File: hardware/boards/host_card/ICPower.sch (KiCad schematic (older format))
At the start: 48 parts, among them J6 SODIMM_260, U1 ECP5UM5G-381caBGA, U3 CYUSB3014, U4 IS43TR16256B-125KBL, U5 128MiB, U6 128MiB, U7 SI5330B

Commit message: Updated the generic SODIMM part footprint to use the new Debug Module footprint
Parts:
- J6: footprint lethalbit-connectors:TE_SODIMM_260 -> lethalbit-connectors:lethallink_Debug_Module_Mount
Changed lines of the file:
@@
 F 0 "J6" H 14400 3525 50  0000 C CNN
 F 1 "SODIMM_260" H 14400 3434 50  0000 C CNN
-F 2 "lethalbit-connectors:TE_SODIMM_260" H 14400 3300 50  0001 C CNN
+F 2 "lethalbit-connectors:lethallink_Debug_Module_Mount" H 14400 3300 50  0001 C CNN
 F 3 "https://www.te.com/commerce/DocumentDelivery/DDEController?Action=srchrtrv&DocNm=2309413&DocType=Customer+Drawing&DocLang=English" H 14400 3300 50  0001 C CNN
 F 4 "TE Connectivity AMP Connectors" H 14400 2950 50  0001 C CNN "MFR"
@@
 F 0 "J6" H 14400 7275 50  0000 C CNN
 F 1 "SODIMM_260" H 14400 7184 50  0000 C CNN
-F 2 "lethalbit-connectors:TE_SODIMM_260" H 14400 7050 50  0001 C CNN
+F 2 "lethalbit-connectors:lethallink_Debug_Module_Mount" H 14400 7050 50  0001 C CNN
 F 3 "https://www.te.com/commerce/DocumentDelivery/DDEController?Action=srchrtrv&DocNm=2309413&DocType=Customer+Drawing&DocLang=English" H 14400 7050 50  0001 C CNN
 F 4 "TE Connectivity AMP Connectors" H 14400 6700 50  0001 C CNN "MFR"

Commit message: Some updates with the debug module interface
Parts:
- J6: footprint lethalbit-connectors:lethallink_Debug_Module_Mount -> lethallink:lethallink_debug_module_mount
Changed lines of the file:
@@
 F 0 "J6" H 14400 3525 50  0000 C CNN
 F 1 "SODIMM_260" H 14400 3434 50  0000 C CNN
-F 2 "lethalbit-connectors:lethallink_Debug_Module_Mount" H 14400 3300 50  0001 C CNN
+F 2 "lethallink:lethallink_debug_module_mount" H 14400 3300 50  0001 C CNN
 F 3 "https://www.te.com/commerce/DocumentDelivery/DDEController?Action=srchrtrv&DocNm=2309413&DocType=Customer+Drawing&DocLang=English" H 14400 3300 50  0001 C CNN
 F 4 "TE Connectivity AMP Connectors" H 14400 2950 50  0001 C CNN "MFR"
@@
 F 0 "J6" H 14400 7275 50  0000 C CNN
 F 1 "SODIMM_260" H 14400 7184 50  0000 C CNN
-F 2 "lethalbit-connectors:lethallink_Debug_Module_Mount" H 14400 7050 50  0001 C CNN
+F 2 "lethallink:lethallink_debug_module_mount" H 14400 7050 50  0001 C CNN
 F 3 "https://www.te.com/commerce/DocumentDelivery/DDEController?Action=srchrtrv&DocNm=2309413&DocType=Customer+Drawing&DocLang=English" H 14400 7050 50  0001 C CNN
 F 4 "TE Connectivity AMP Connectors" H 14400 6700 50  0001 C CNN "MFR"

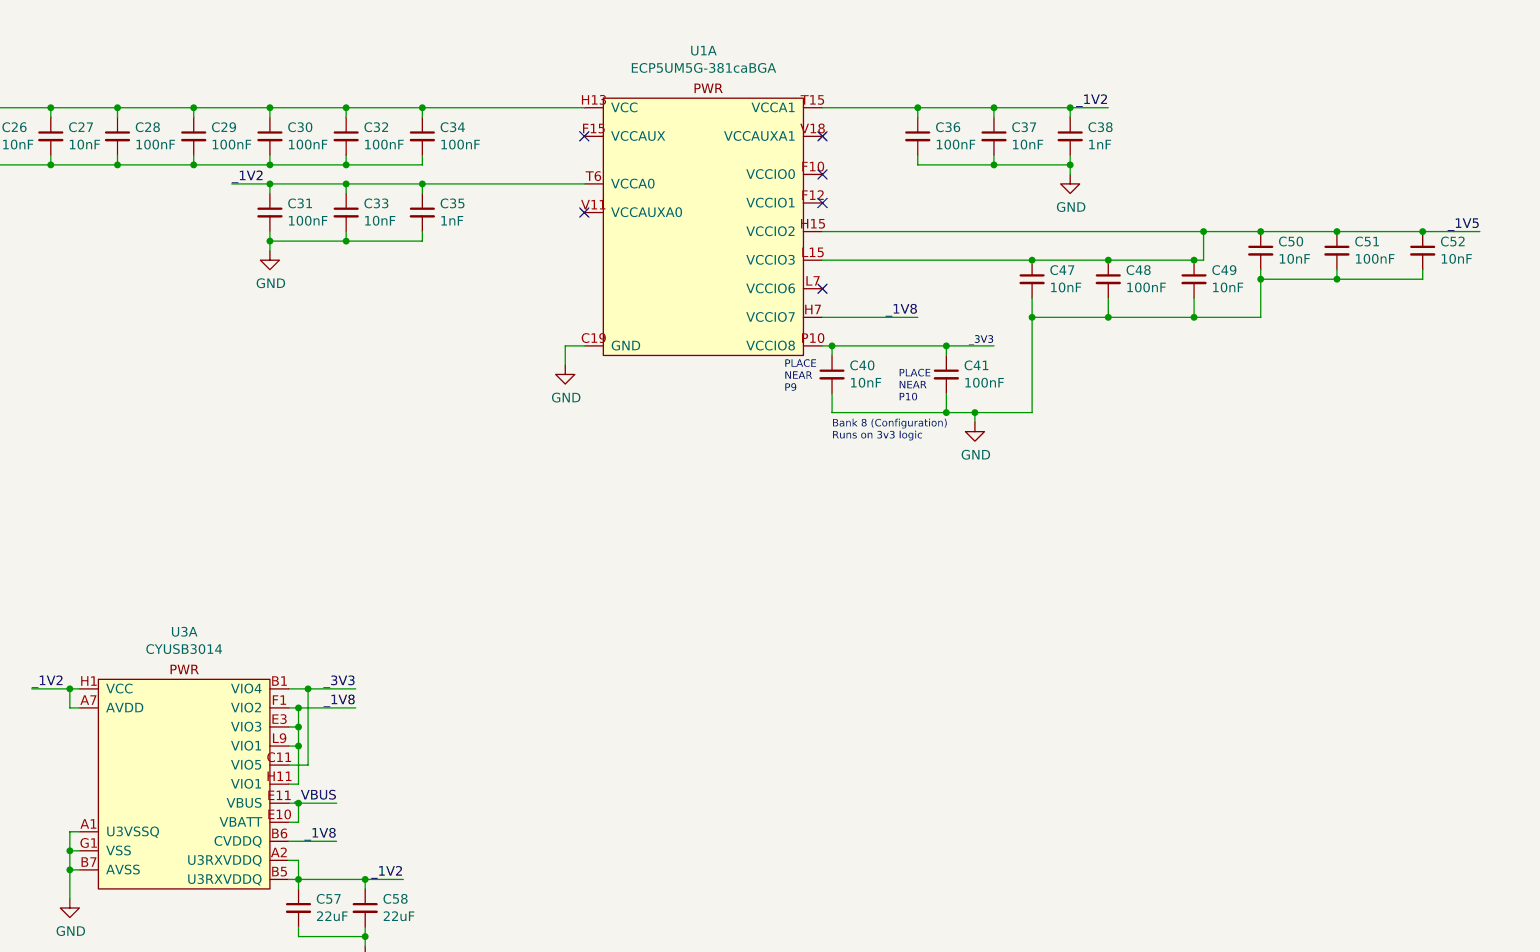
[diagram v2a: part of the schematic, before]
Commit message: Fixed up the consistancy of value naming, 100nF -> 0.1uF. Added the caps for the USB SSRX lines, moved the Ferrite for VBUS to fix a net naming issue
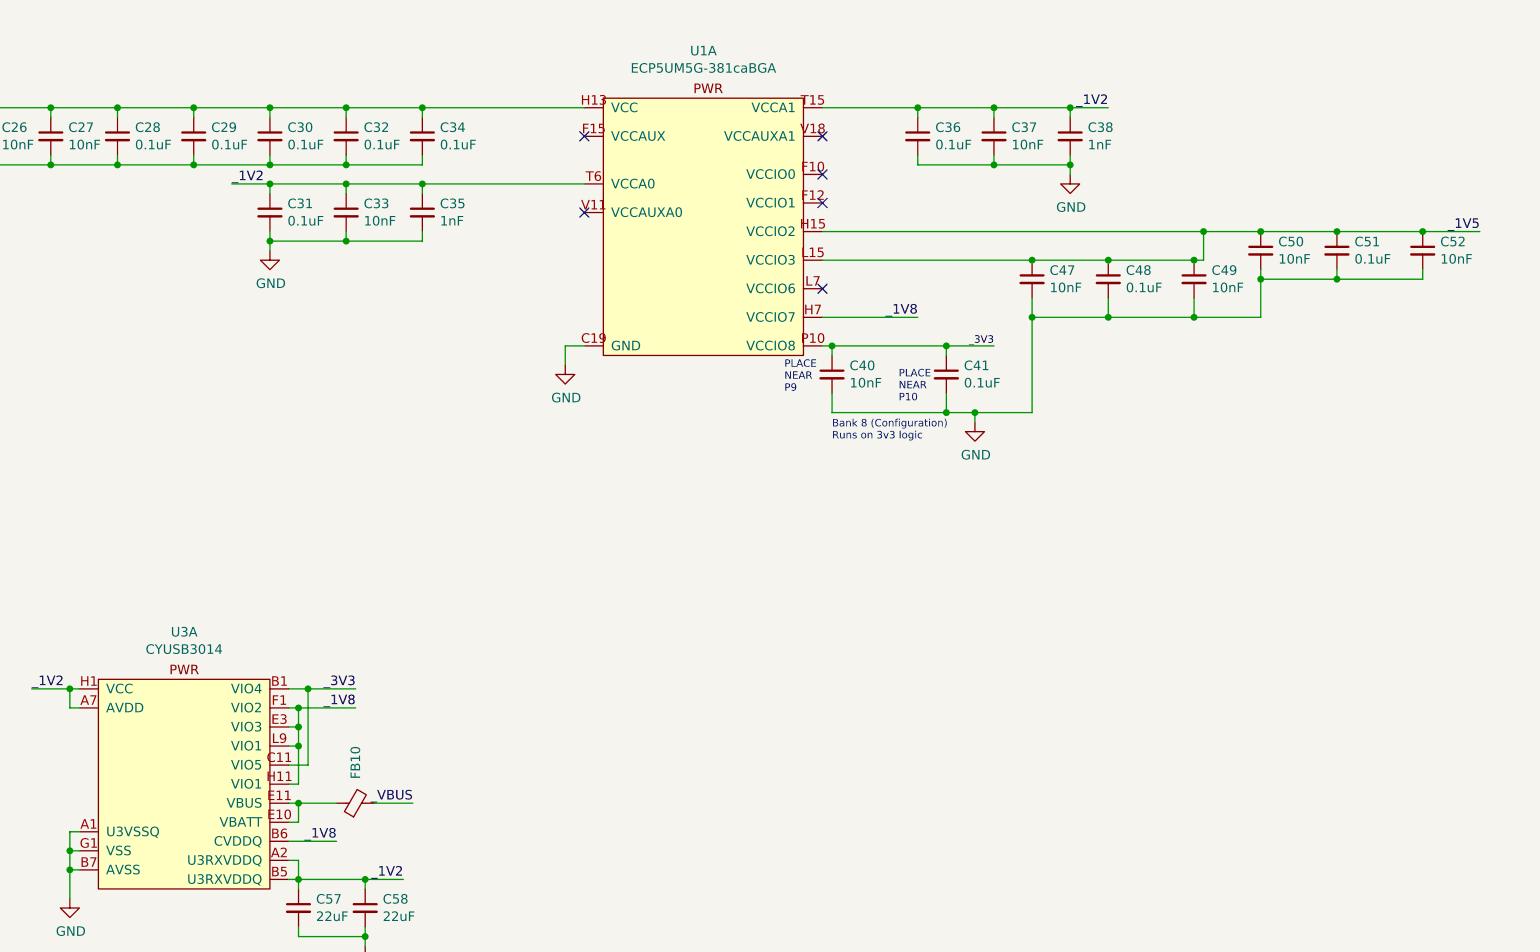
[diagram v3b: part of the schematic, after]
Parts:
- added FB10: 220 @ 100Mhz, Resistor_SMD:R_0603_1608Metric, symbol Device:Ferrite_Bead_Small
- C28, C29, C30, C31, C32, C34, C36, C41, C48, C51: value 100nF -> 0.1uF
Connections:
- net VBUS: now also FB10.2; no longer U3.E10 (VBATT), U3.E11 (VBUS)
- new net: FB10.1, U3.E10 (VBATT), U3.E11 (VBUS)
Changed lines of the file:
@@
 P 6200 2200
 F 0 "C31" H 6292 2246 50  0000 L CNN
-F 1 "100nF" H 6292 2155 50  0000 L CNN
+F 1 "0.1uF" H 6292 2155 50  0000 L CNN
 F 2 "Capacitor_SMD:C_0402_1005Metric" H 6200 2200 50  0001 C CNN
 F 3 "~" H 6200 2200 50  0001 C CNN
@@
 P 9600 1800
 F 0 "C36" H 9692 1846 50  0000 L CNN
-F 1 "100nF" H 9692 1755 50  0000 L CNN
+F 1 "0.1uF" H 9692 1755 50  0000 L CNN
 F 2 "Capacitor_SMD:C_0402_1005Metric" H 9600 1800 50  0001 C CNN
 F 3 "~" H 9600 1800 50  0001 C CNN
@@
 P 7000 1800
 F 0 "C34" H 7092 1846 50  0000 L CNN
-F 1 "100nF" H 7092 1755 50  0000 L CNN
+F 1 "0.1uF" H 7092 1755 50  0000 L CNN
 F 2 "Capacitor_SMD:C_0402_1005Metric" H 7000 1800 50  0001 C CNN
 F 3 "~" H 7000 1800 50  0001 C CNN
@@
 P 6600 1800
 F 0 "C32" H 6692 1846 50  0000 L CNN
-F 1 "100nF" H 6692 1755 50  0000 L CNN
+F 1 "0.1uF" H 6692 1755 50  0000 L CNN
 F 2 "Capacitor_SMD:C_0402_1005Metric" H 6600 1800 50  0001 C CNN
 F 3 "~" H 6600 1800 50  0001 C CNN
@@
 P 6200 1800
 F 0 "C30" H 6292 1846 50  0000 L CNN
-F 1 "100nF" H 6292 1755 50  0000 L CNN
+F 1 "0.1uF" H 6292 1755 50  0000 L CNN
 F 2 "Capacitor_SMD:C_0402_1005Metric" H 6200 1800 50  0001 C CNN
 F 3 "~" H 6200 1800 50  0001 C CNN
@@
 P 5800 1800
 F 0 "C29" H 5892 1846 50  0000 L CNN
-F 1 "100nF" H 5892 1755 50  0000 L CNN
+F 1 "0.1uF" H 5892 1755 50  0000 L CNN
 F 2 "Capacitor_SMD:C_0402_1005Metric" H 5800 1800 50  0001 C CNN
 F 3 "~" H 5800 1800 50  0001 C CNN
@@
 P 5400 1800
 F 0 "C28" H 5492 1846 50  0000 L CNN
-F 1 "100nF" H 5492 1755 50  0000 L CNN
+F 1 "0.1uF" H 5492 1755 50  0000 L CNN
 F 2 "Capacitor_SMD:C_0402_1005Metric" H 5400 1800 50  0001 C CNN
 F 3 "~" H 5400 1800 50  0001 C CNN
@@
 P 9750 3050
 F 0 "C41" H 9842 3096 50  0000 L CNN
-F 1 "100nF" H 9842 3005 50  0000 L CNN
+F 1 "0.1uF" H 9842 3005 50  0000 L CNN
 F 2 "Capacitor_SMD:C_0402_1005Metric" H 9750 3050 50  0001 C CNN
 F 3 "~" H 9750 3050 50  0001 C CNN
@@
 Wire Wire Line
 	6300 5300 6350 5300
-Text Label 6550 5300 2    50   ~ 0
-_VBUS
 $Comp
 L power:GND #PWR0124
@@
 P 10600 2550
 F 0 "C48" H 10692 2596 50  0000 L CNN
-F 1 "100nF" H 10692 2505 50  0000 L CNN
+F 1 "0.1uF" H 10692 2505 50  0000 L CNN
 F 2 "Capacitor_SMD:C_0402_1005Metric" H 10600 2550 50  0001 C CNN
 F 3 "~" H 10600 2550 50  0001 C CNN
@@
 P 11800 2400
 F 0 "C51" H 11892 2446 50  0000 L CNN
-F 1 "100nF" H 11892 2355 50  0000 L CNN
+F 1 "0.1uF" H 11892 2355 50  0000 L CNN
 F 2 "Capacitor_SMD:C_0402_1005Metric" H 11800 2400 50  0001 C CNN
 F 3 "~" H 11800 2400 50  0001 C CNN
@@
 Wire Wire Line
 	6350 5400 6300 5400
-Connection ~ 6350 5300
-Wire Wire Line
-	6350 5300 6550 5300
 Wire Wire Line
 	6300 5100 6400 5100
@@
 	1    0    0    -1
 $EndComp
+$Comp
+L Device:Ferrite_Bead_Small FB?
+U 1 1 5F3AE682
+P 6650 5300
+AR Path="/5F3AE682" Ref="FB?"  Part="1"
+AR Path="/5EF66188/5F3AE682" Ref="FB10"  Part="1"
+F 0 "FB10" H 6950 5300 50  0000 R CNN
+F 1 "220 @ 100Mhz" H 6800 5500 50  0001 R CNN
+F 2 "Resistor_SMD:R_0603_1608Metric" V 6580 5300 50  0001 C CNN
+F 3 "~" H 6650 5300 50  0001 C CNN
+F 4 "Murata Electronics" H 6650 5300 50  0001 C CNN "MFR"
+F 5 "BLM18AG221SN1D" H 6650 5300 50  0001 C CNN "MPN"
+	1    6650 5300
+	0    -1   -1   0
+$EndComp
+Text Label 6950 5300 2    50   ~ 0
+_VBUS
+Wire Wire Line
+	6750 5300 6950 5300
+Wire Wire Line
+	6350 5300 6550 5300
+Connection ~ 6350 5300
 $EndSCHEMATC

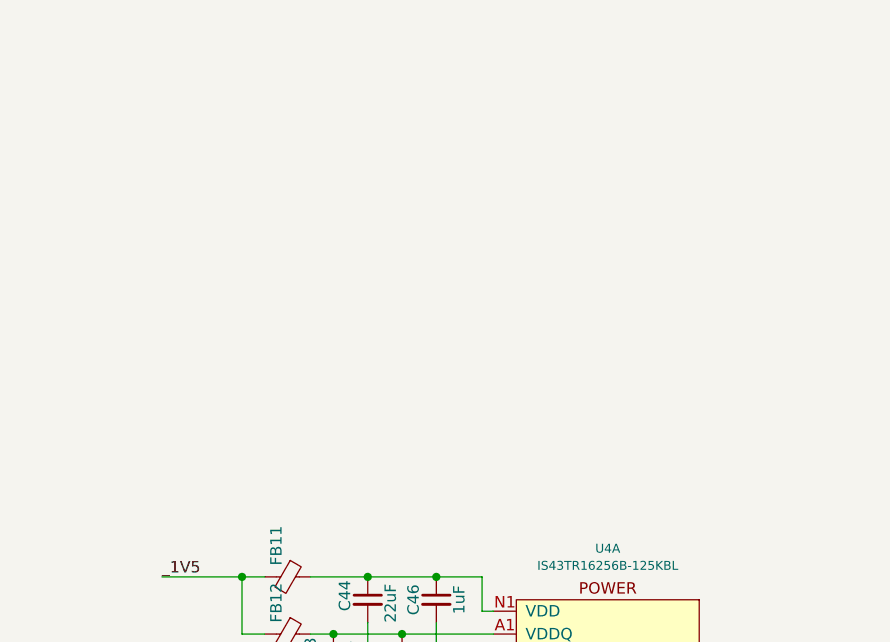
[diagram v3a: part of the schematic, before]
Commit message: Added another DDR3 module to expand cache to 8GiB
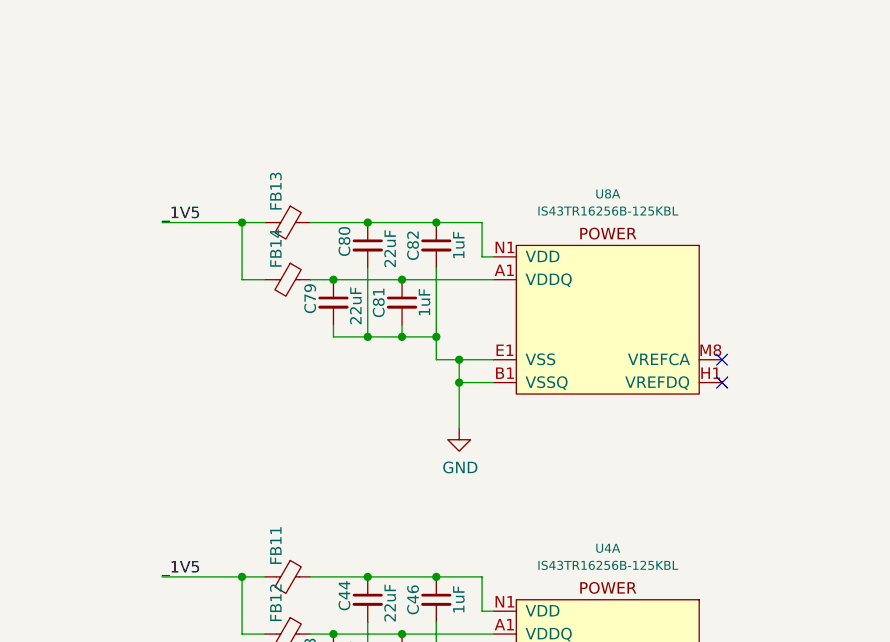
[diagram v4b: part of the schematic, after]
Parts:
- added C79, C80: 22uF, Capacitor_SMD:C_1206_3216Metric, symbol Device:C_Small
- added C81, C82: 1uF, Capacitor_SMD:C_0603_1608Metric, symbol Device:C_Small
- added FB13, FB14: 220 @ 100Mhz, Resistor_SMD:R_0603_1608Metric, symbol Device:Ferrite_Bead_Small
- added U8: IS43TR16256B-125KBL, Package_BGA:BGA-96_9.0x13.0mm_Layout2x3x16_P0.8mm, symbol lethalbit-memory:IS43TR16256B-125KBL
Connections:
- net 1V5: now also FB13.2, FB14.2
- net GND: now also C79.2, C80.2, C81.2, C82.2, U8.A9 (VSS), U8.B1 (VSSQ), U8.B3 (VSS), U8.B9 (VSSQ), U8.D1 (VSSQ), U8.D8 (VSSQ), U8.E1 (VSS), U8.E2 (VSSQ), U8.E8 (VSSQ), U8.F9 (VSSQ), U8.G1 (VSSQ), U8.G8 (VSS), U8.G9 (VSSQ), U8.J2 (VSS), U8.J8 (VSS), U8.M1 (VSS), U8.M9 (VSS), U8.P1 (VSS), U8.P9 (VSS), U8.T1 (VSS), U8.T9 (VSS)
- new net: C79.1, C81.1, FB14.1, U8.A1 (VDDQ), U8.A8 (VDDQ), U8.C1 (VDDQ), U8.C9 (VDDQ), U8.D2 (VDDQ), U8.E9 (VDDQ), U8.F1 (VDDQ), U8.H2 (VDDQ), U8.H9 (VDDQ)
- new net: C80.1, C82.1, FB13.1, U8.B2 (VDD), U8.D9 (VDD), U8.G7 (VDD), U8.K2 (VDD), U8.K8 (VDD), U8.N1 (VDD), U8.N9 (VDD), U8.R1 (VDD), U8.R9 (VDD)
- no-connect marks 8 -> 10
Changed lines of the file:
@@
 	6350 5300 6550 5300
 Connection ~ 6350 5300
+$Comp
+L lethalbit-memory:IS43TR16256B-125KBL U8
+U 1 1 5F484D89
+P 10250 6650
+F 0 "U8" H 10250 7124 39  0000 C CNN
+F 1 "IS43TR16256B-125KBL" H 10250 7049 39  0000 C CNN
+F 2 "Package_BGA:BGA-96_9.0x13.0mm_Layout2x3x16_P0.8mm" H 10250 7050 39  0001 C CNN
+F 3 "http://www.issi.com/WW/pdf/43-46TR16256B-85120BL.pdf" H 10250 7050 39  0001 C CNN
+F 4 "ISSI" H 10250 6650 50  0001 C CNN "MFR"
+F 5 "IS43TR16256B-125KBL" H 10250 6650 50  0001 C CNN "MPN"
+	1    10250 6650
+	1    0    0    -1
+$EndComp
+$Comp
+L power:GND #PWR0145
+U 1 1 5F4B038F
+P 9600 7200
+F 0 "#PWR0145" H 9600 6950 50  0001 C CNN
+F 1 "GND" H 9605 7027 50  0000 C CNN
+F 2 "" H 9600 7200 50  0001 C CNN
+F 3 "" H 9600 7200 50  0001 C CNN
+	1    9600 7200
+	1    0    0    -1
+$EndComp
+Wire Wire Line
+	9750 7000 9600 7000
+Wire Wire Line
+	9600 7000 9600 7200
+Wire Wire Line
+	9750 6900 9600 6900
+Wire Wire Line
+	9600 6900 9600 7000
+Connection ~ 9600 7000
+Wire Wire Line
+	8650 6550 8650 6300
+Wire Wire Line
+	8650 6300 8300 6300
+Text Label 8300 6300 0    50   ~ 0
+_1V5
+Wire Wire Line
+	8750 6550 8650 6550
+Wire Wire Line
+	8650 6300 8750 6300
+Connection ~ 8650 6300
+$Comp
+L Device:Ferrite_Bead_Small FB?
+U 1 1 5F4B03A2
+P 8850 6550
+AR Path="/5F4B03A2" Ref="FB?"  Part="1"
+AR Path="/5EF66188/5F4B03A2" Ref="FB14"  Part="1"
+F 0 "FB14" H 8800 6500 50  0000 R CNN
+F 1 "220 @ 100Mhz" H 9000 6750 50  0001 R CNN
+F 2 "Resistor_SMD:R_0603_1608Metric" V 8780 6550 50  0001 C CNN
+F 3 "~" H 8850 6550 50  0001 C CNN
+F 4 "Murata Electronics" H 8850 6550 50  0001 C CNN "MFR"
+F 5 "BLM18AG221SN1D" H 8850 6550 50  0001 C CNN "MPN"
+	1    8850 6550
+	0    1    1    0
+$EndComp
+$Comp
+L Device:Ferrite_Bead_Small FB?
+U 1 1 5F4B03AA
+P 8850 6300
+AR Path="/5F4B03AA" Ref="FB?"  Part="1"
+AR Path="/5EF66188/5F4B03AA" Ref="FB13"  Part="1"
+F 0 "FB13" H 8800 6250 50  0000 R CNN
+F 1 "220 @ 100Mhz" H 9000 6500 50  0001 R CNN
+F 2 "Resistor_SMD:R_0603_1608Metric" V 8780 6300 50  0001 C CNN
+F 3 "~" H 8850 6300 50  0001 C CNN
+F 4 "Murata Electronics" H 8850 6300 50  0001 C CNN "MFR"
+F 5 "BLM18AG221SN1D" H 8850 6300 50  0001 C CNN "MPN"
+	1    8850 6300
+	0    1    1    0
+$EndComp
+Wire Wire Line
+	8950 6550 9050 6550
+Wire Wire Line
+	9700 6300 9700 6450
+Wire Wire Line
+	9700 6450 9750 6450
+$Comp
+L Device:C_Small C?
+U 1 1 5F4B03B5
+P 9050 6650
+AR Path="/5EDF9F51/5F4B03B5" Ref="C?"  Part="1"
+AR Path="/5EF66188/5F4B03B5" Ref="C79"  Part="1"
+F 0 "C79" V 8950 6600 50  0000 L CNN
+F 1 "22uF" V 9150 6550 50  0000 L CNN
+F 2 "Capacitor_SMD:C_1206_3216Metric" H 9050 6650 50  0001 C CNN
+F 3 "~" H 9050 6650 50  0001 C CNN
+F 4 "KEMET" H 9050 6650 50  0001 C CNN "MFR"
+F 5 "C1206C226K9PACTU" H 9050 6650 50  0001 C CNN "MPN"
+	1    9050 6650
+	1    0    0    -1
+$EndComp
+Connection ~ 9050 6550
+Wire Wire Line
+	9050 6550 9350 6550
+$Comp
+L Device:C_Small C?
+U 1 1 5F4B03BF
+P 9350 6650
+AR Path="/5EDF9F51/5F4B03BF" Ref="C?"  Part="1"
+AR Path="/5EF66188/5F4B03BF" Ref="C81"  Part="1"
+F 0 "C81" V 9250 6650 50  0000 C CNN
+F 1 "1uF" V 9450 6650 50  0000 C CNN
+F 2 "Capacitor_SMD:C_0603_1608Metric" H 9350 6650 50  0001 C CNN
+F 3 "~" H 9350 6650 50  0001 C CNN
+F 4 "KEMET" V 9350 6650 50  0001 C CNN "MFR"
+F 5 "C0603C105K4RACTU" V 9350 6650 50  0001 C CNN "MPN"
+	1    9350 6650
+	1    0    0    -1
+$EndComp
+Connection ~ 9350 6550
+Wire Wire Line
+	9350 6550 9750 6550
+Wire Wire Line
+	8950 6300 9200 6300
+$Comp
+L Device:C_Small C?
+U 1 1 5F4B03CA
+P 9200 6400
+AR Path="/5EDF9F51/5F4B03CA" Ref="C?"  Part="1"
+AR Path="/5EF66188/5F4B03CA" Ref="C80"  Part="1"
+F 0 "C80" V 9100 6350 50  0000 L CNN
+F 1 "22uF" V 9300 6300 50  0000 L CNN
+F 2 "Capacitor_SMD:C_1206_3216Metric" H 9200 6400 50  0001 C CNN
+F 3 "~" H 9200 6400 50  0001 C CNN
+F 4 "KEMET" H 9200 6400 50  0001 C CNN "MFR"
+F 5 "C1206C226K9PACTU" H 9200 6400 50  0001 C CNN "MPN"
+	1    9200 6400
+	1    0    0    -1
+$EndComp
+$Comp
+L Device:C_Small C?
+U 1 1 5F4B03D2
+P 9500 6400
+AR Path="/5EDF9F51/5F4B03D2" Ref="C?"  Part="1"
+AR Path="/5EF66188/5F4B03D2" Ref="C82"  Part="1"
+F 0 "C82" V 9400 6400 50  0000 C CNN
+F 1 "1uF" V 9600 6400 50  0000 C CNN
+F 2 "Capacitor_SMD:C_0603_1608Metric" H 9500 6400 50  0001 C CNN
+F 3 "~" H 9500 6400 50  0001 C CNN
+F 4 "KEMET" V 9500 6400 50  0001 C CNN "MFR"
+F 5 "C0603C105K4RACTU" V 9500 6400 50  0001 C CNN "MPN"
+	1    9500 6400
+	1    0    0    -1
+$EndComp
+Connection ~ 9200 6300
+Wire Wire Line
+	9200 6300 9500 6300
+Connection ~ 9500 6300
+Wire Wire Line
+	9500 6300 9700 6300
+Wire Wire Line
+	9050 6750 9050 6800
+Wire Wire Line
+	9050 6800 9200 6800
+Wire Wire Line
+	9350 6800 9350 6750
+Wire Wire Line
+	9200 6500 9200 6800
+Connection ~ 9200 6800
+Wire Wire Line
+	9200 6800 9350 6800
+Wire Wire Line
+	9500 6500 9500 6800
+Wire Wire Line
+	9500 6800 9350 6800
+Connection ~ 9350 6800
+Wire Wire Line
+	9500 6800 9500 6900
+Wire Wire Line
+	9500 6900 9600 6900
+Connection ~ 9500 6800
+Connection ~ 9600 6900
+NoConn ~ 10750 6900
+NoConn ~ 10750 7000
 $EndSCHEMATC

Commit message: Fixed  / updated the ECP5 symbol for the ECP5UM5G-85K
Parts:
- U1: symbol lethalbit:ECP5UM5G-381caBGA -> lethalbit:LFE5UM5G-85F-8BG381I
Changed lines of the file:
@@
 $EndDescr
 $Comp
-L lethalbit:ECP5UM5G-381caBGA U?
+L lethalbit:LFE5UM5G-85F-8BG381I U?
 U 1 1 5F21FED7
 P 8500 1700
